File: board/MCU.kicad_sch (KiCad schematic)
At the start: 27 parts, among them J1 DEBUG, Q1 NMOS, Q2 BSS138, U4 LT1910, U7 ESP32-S2-DEVKITM-1U

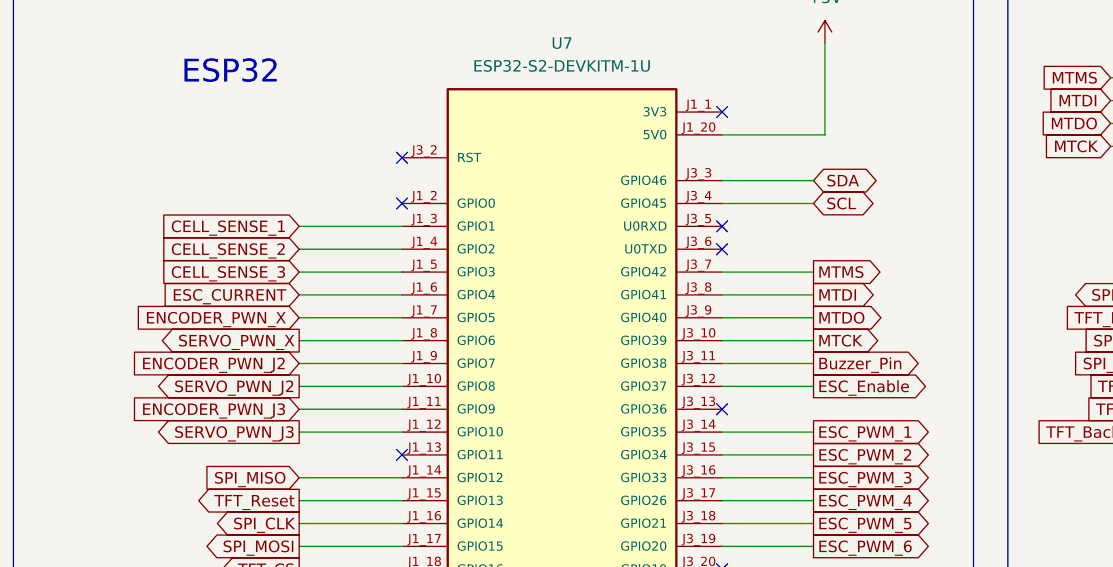
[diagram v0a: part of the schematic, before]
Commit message: fixed a few small issues on layout
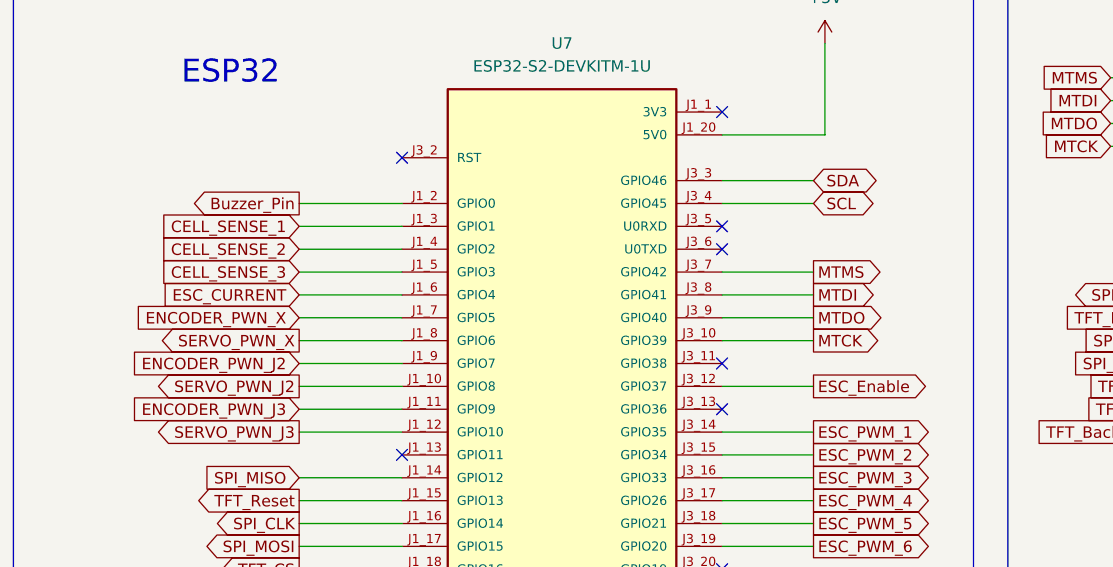
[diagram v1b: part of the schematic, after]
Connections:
- net Buzzer_Pin: now also U7.J1_2 (GPIO0); no longer U7.J3_11 (GPIO38)

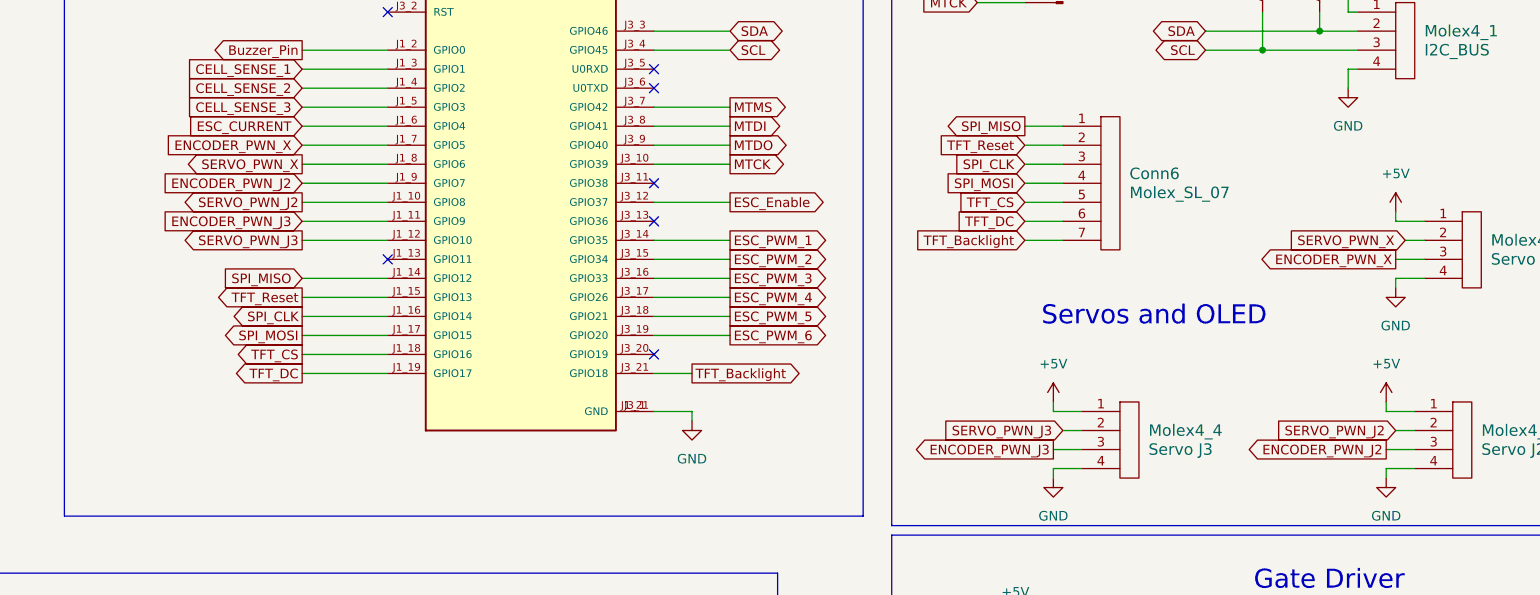
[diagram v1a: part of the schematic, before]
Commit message: Add 12 volt trace
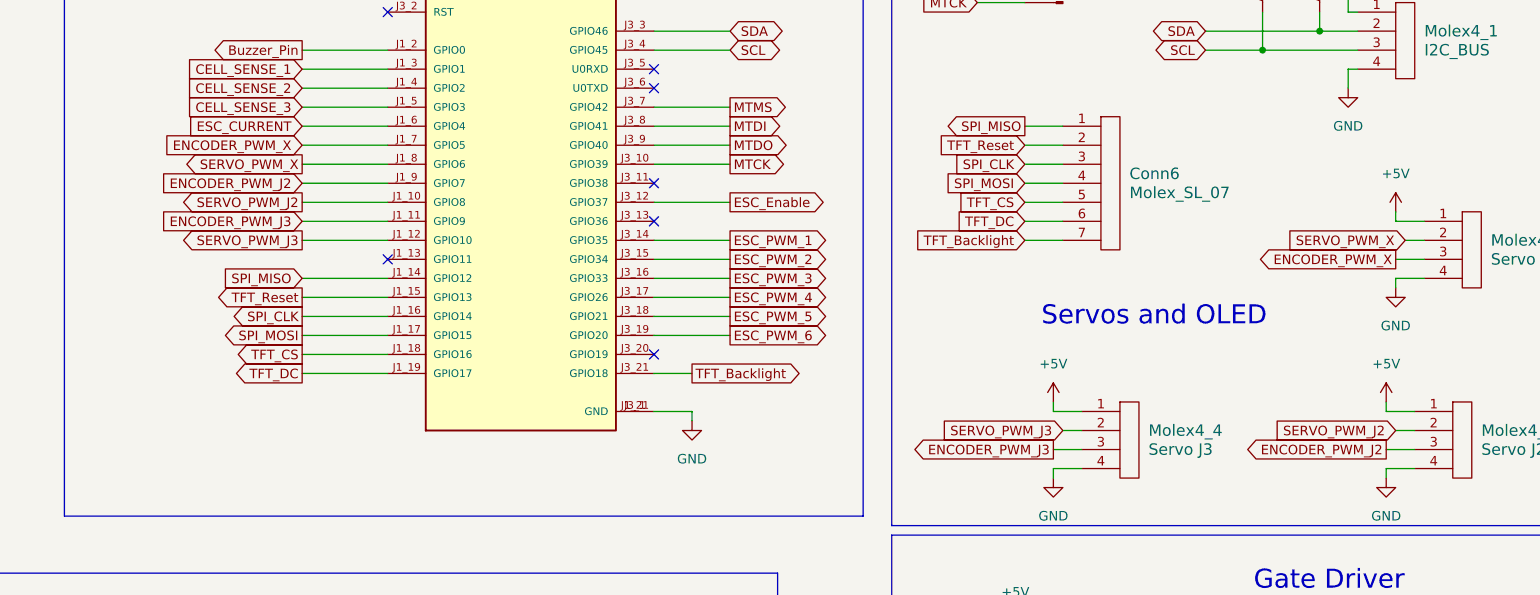
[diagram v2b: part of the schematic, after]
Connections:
- net ENCODER_PWN_J2 renamed ENCODER_PWM_J2
- net ENCODER_PWN_J3 renamed ENCODER_PWM_J3
- net ENCODER_PWN_X renamed ENCODER_PWM_X
- net SERVO_PWN_J2 renamed SERVO_PWM_J2
- net SERVO_PWN_J3 renamed SERVO_PWM_J3
- net SERVO_PWN_X renamed SERVO_PWM_X

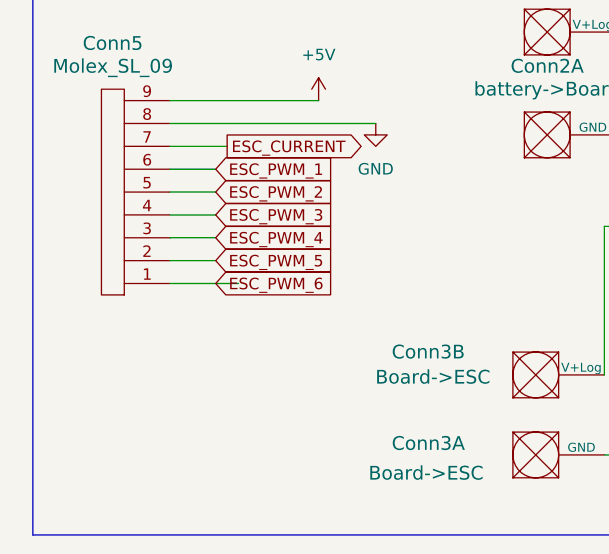
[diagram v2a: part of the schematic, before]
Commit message: Add unconnected trace on OpAmp Net
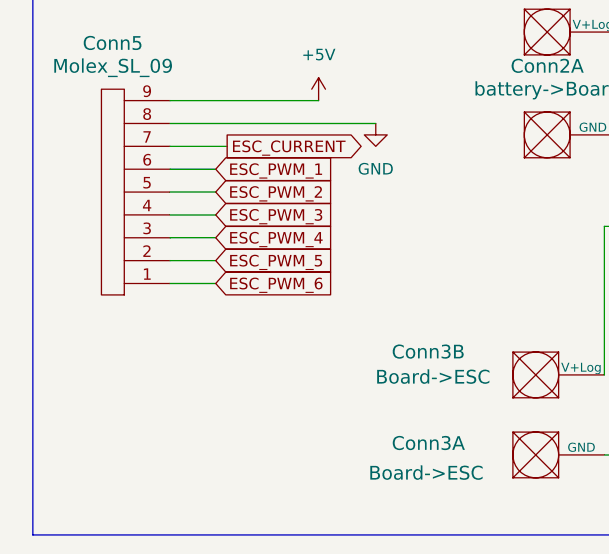
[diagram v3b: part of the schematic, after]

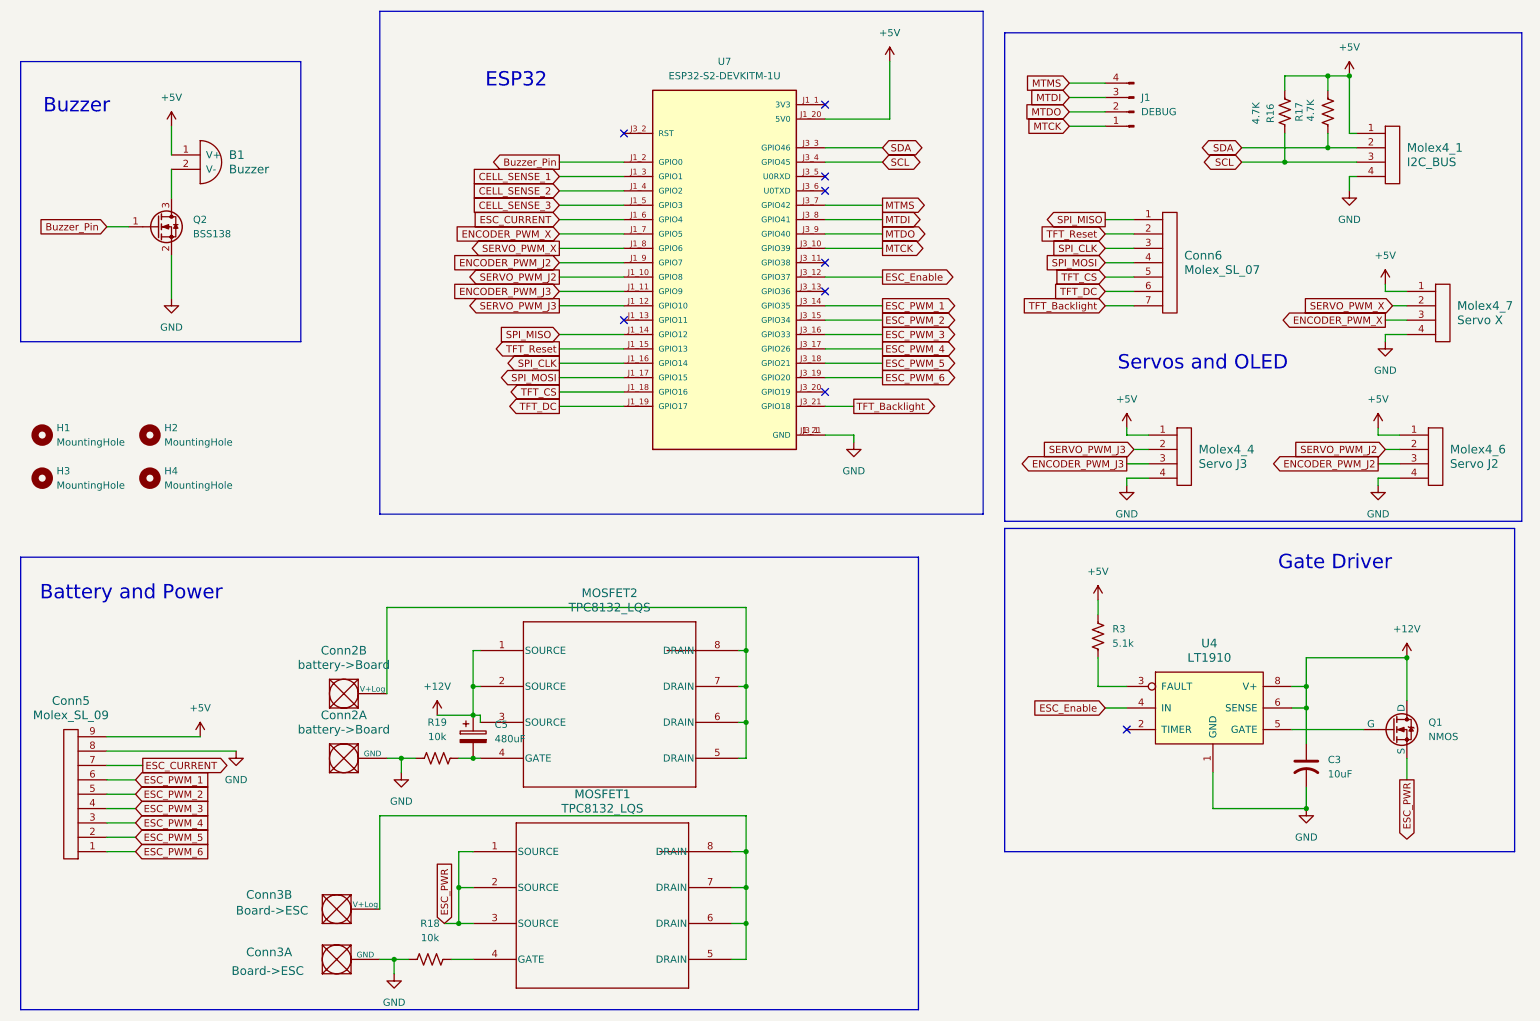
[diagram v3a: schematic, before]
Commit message: Add ESTOP
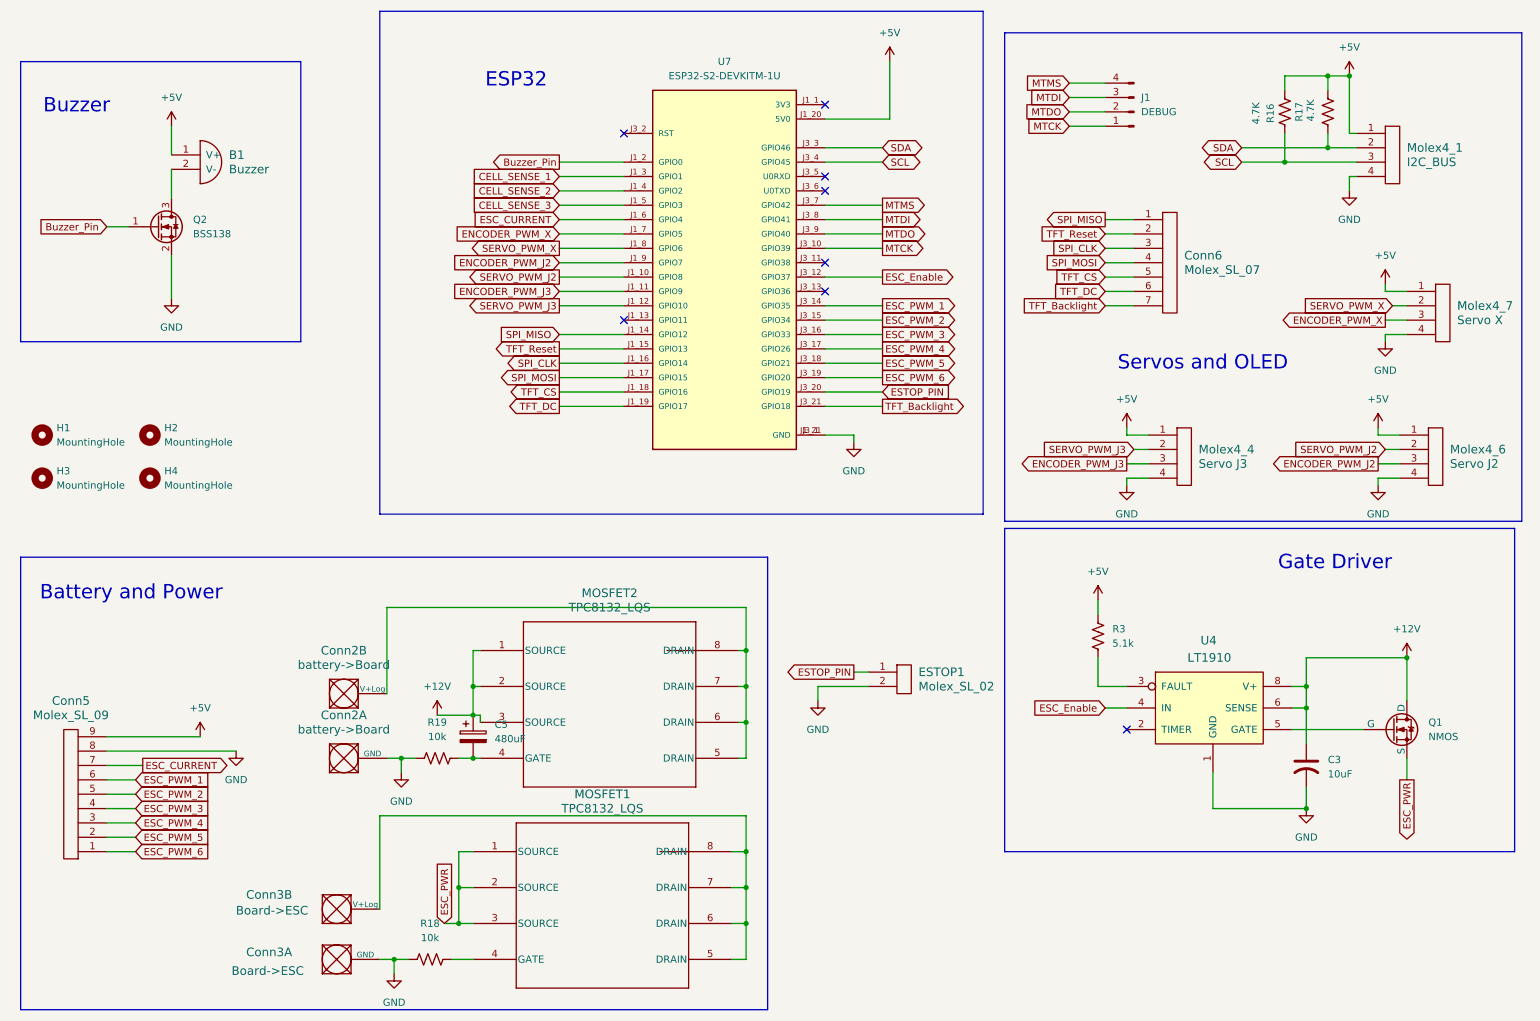
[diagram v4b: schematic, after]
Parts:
- added ESTOP1: Molex_SL_02, MRDT_Connectors:MOLEX_SL_02_Vertical, symbol MRDT_Connectors:Molex_SL_02
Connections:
- net GND: now also ESTOP1.2
- net ESTOP_PIN: now reaches U7.J3_20 (GPIO19)
- net ESTOP_PIN: now also ESTOP1.1
- no-connect marks 9 -> 8

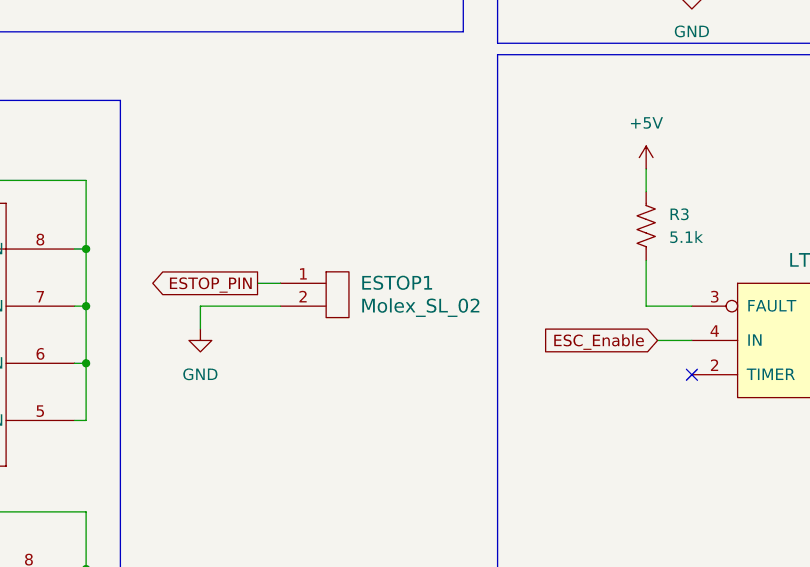
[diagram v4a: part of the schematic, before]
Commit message: Add Estop & ESP32 footprint
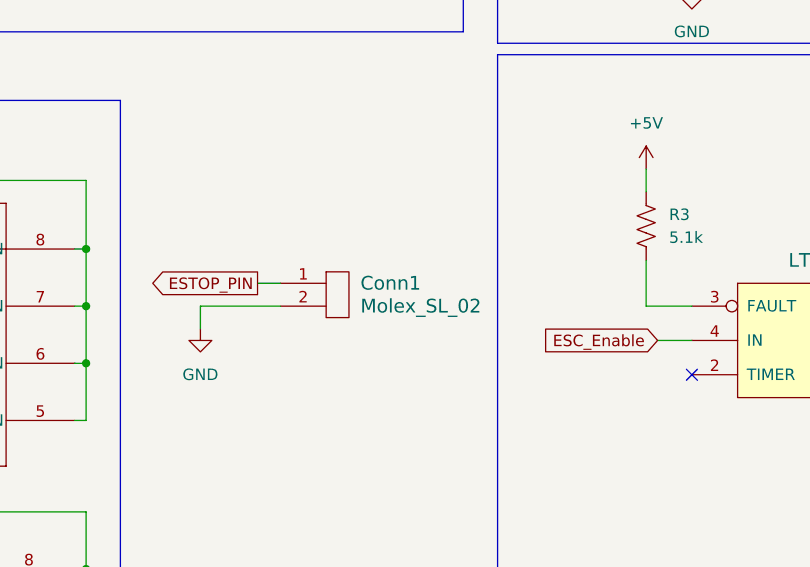
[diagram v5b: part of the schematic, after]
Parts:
- removed ESTOP1: Molex_SL_02, MRDT_Connectors:MOLEX_SL_02_Vertical, symbol MRDT_Connectors:Molex_SL_02
- added Conn1: Molex_SL_02, MRDT_Connectors:MOLEX_SL_02_Vertical, symbol MRDT_Connectors:Molex_SL_02
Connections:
- net ESTOP_PIN: now also Conn1.1
- net GND: now also Conn1.2

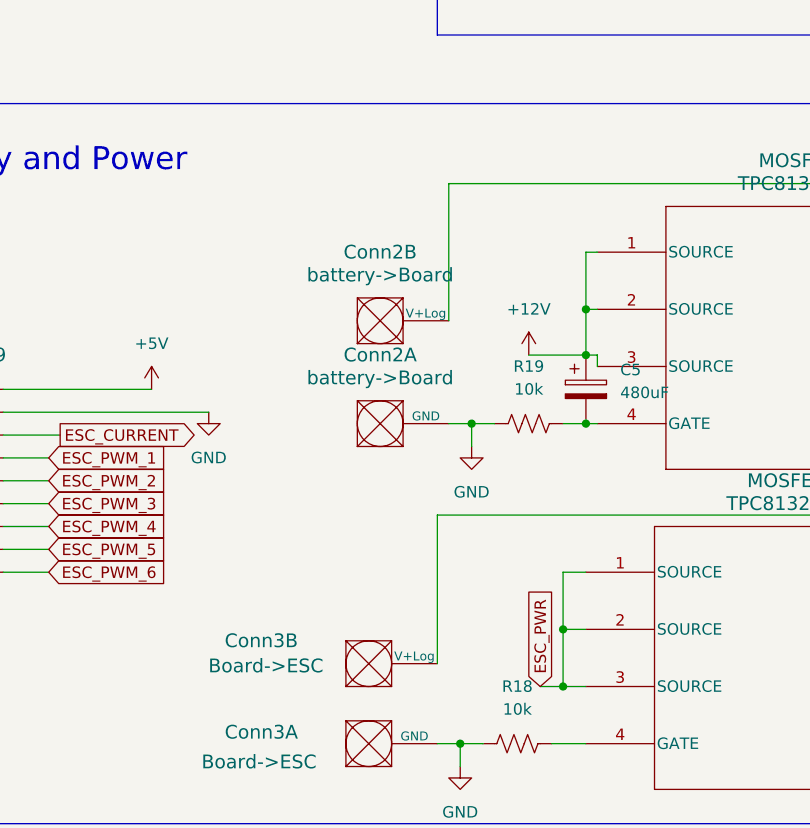
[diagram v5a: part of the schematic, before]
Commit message: Fix mounting holes, anderson net, add MRDT silkscreen
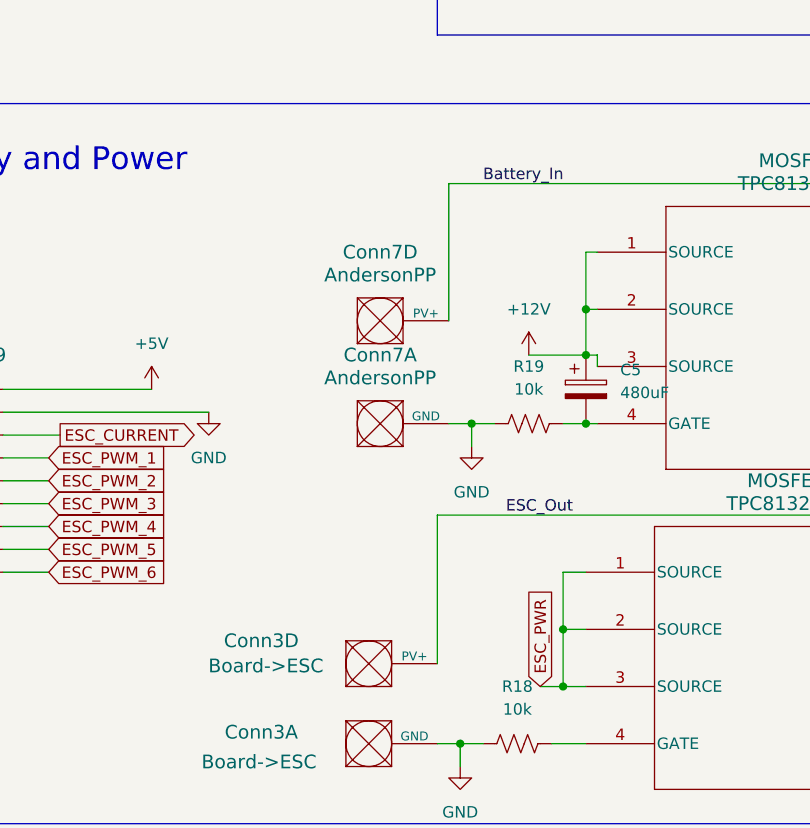
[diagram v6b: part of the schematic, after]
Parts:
- removed Conn2: battery->Board, MRDT_Connectors:Square_Anderson_2_H_Side_By_Side_PV, symbol MRDT_Connectors:AndersonPP
- added Conn7: AndersonPP, MRDT_Connectors:Square_Anderson_2_H_Side_By_Side_PV, symbol MRDT_Connectors:AndersonPP
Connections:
- net GND: now also Conn7.1 (GND)
- net Battery_In: now reaches MOSFET2.5 (DRAIN), MOSFET2.6 (DRAIN), MOSFET2.7 (DRAIN), MOSFET2.8 (DRAIN)
- net Battery_In: now also Conn7.4 (PV+)
- net ESC_Out: now reaches MOSFET1.5 (DRAIN), MOSFET1.6 (DRAIN), MOSFET1.7 (DRAIN), MOSFET1.8 (DRAIN)
- net ESC_Out: now also Conn3.4 (PV+); no longer Conn3.2 (V+Log)
